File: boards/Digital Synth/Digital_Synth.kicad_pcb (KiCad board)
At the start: 2 copper layers, 109 parts, among them J1 AudioJack3, J2 AudioJack3, J3 DIN-5, J4 DIN-5, SW1 C3, SW10 A4, SW11 A#4, SW12 B4, SW13 C4, SW14 C#4, SW15 D4, SW16 D#4, SW17 E4, SW18 F4, SW19 F#4, SW2 C#3, SW20 G4, SW21 G#4, SW22 A5, SW23 A#4, SW24 B5, SW25 C5, SW3 D3, SW4 D#3, SW5 E3, SW6 F3, SW7 F#3, SW8 G3, SW9 G#3, U1 STM32F446RETx, U2 SN74LVC2G14, U3 PCM5101A, U4 6N138

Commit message: laid out keyboard
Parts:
- removed D31, D32, D33, D34, D35, D36, D37, D38, D39, D40, D41, D42, D43, D44, D45, D46, D47, D48, D49, D50, D51, D52, D53, D54, D55: D_Small, Diode_SMD:D_0805_2012Metric_Pad1.15x1.40mm_HandSolder
- removed R9: 220, Resistor_SMD:R_0805_2012Metric_Pad1.15x1.40mm_HandSolder
- removed SW1: C3, Keyswitches:Kailh_socket_MX
- removed SW10: A4, Keyswitches:Kailh_socket_MX
- removed SW11, SW23: A#4, Keyswitches:Kailh_socket_MX
- removed SW12: B4, Keyswitches:Kailh_socket_MX
- removed SW13: C4, Keyswitches:Kailh_socket_MX
- removed SW14: C#4, Keyswitches:Kailh_socket_MX
- removed SW15: D4, Keyswitches:Kailh_socket_MX
- removed SW16: D#4, Keyswitches:Kailh_socket_MX
- removed SW17: E4, Keyswitches:Kailh_socket_MX
- removed SW18: F4, Keyswitches:Kailh_socket_MX
- removed SW19: F#4, Keyswitches:Kailh_socket_MX
- removed SW2: C#3, Keyswitches:Kailh_socket_MX
- removed SW20: G4, Keyswitches:Kailh_socket_MX
- removed SW21: G#4, Keyswitches:Kailh_socket_MX
- removed SW22: A5, Keyswitches:Kailh_socket_MX
- removed SW24: B5, Keyswitches:Kailh_socket_MX
- removed SW25: C5, Keyswitches:Kailh_socket_MX
- removed SW3: D3, Keyswitches:Kailh_socket_MX
- removed SW4: D#3, Keyswitches:Kailh_socket_MX
- removed SW5: E3, Keyswitches:Kailh_socket_MX
- removed SW6: F3, Keyswitches:Kailh_socket_MX
- removed SW7: F#3, Keyswitches:Kailh_socket_MX
- removed SW8: G3, Keyswitches:Kailh_socket_MX
- removed SW9: G#3, Keyswitches:Kailh_socket_MX
- removed U1: STM32F446RETx, Package_QFP:LQFP-64_10x10mm_P0.5mm
- added C1: 0.1uF, Capacitor_SMD:C_0603_1608Metric_Pad1.05x0.95mm_HandSolder, F.Cu at (78.1, -9.42)
- added C15: 0.1uF, Capacitor_SMD:C_0603_1608Metric_Pad1.05x0.95mm_HandSolder, B.Cu at (157.6, -9.27)
- added C17: 0.1uF, Capacitor_SMD:C_0603_1608Metric_Pad1.05x0.95mm_HandSolder, B.Cu at (154.9, -13.1)
- added C21: 0.1uF, Capacitor_SMD:C_0603_1608Metric_Pad1.05x0.95mm_HandSolder, B.Cu at (154.9, -18.0)
- added C26: 0.1uF, Capacitor_SMD:C_0603_1608Metric_Pad1.05x0.95mm_HandSolder, B.Cu at (157.1, -20.8)
- added C27: 0.1uF, Capacitor_SMD:C_0603_1608Metric_Pad1.05x0.95mm_HandSolder, B.Cu at (166.4, -18.4)
- added C28: 0.1uF, Capacitor_SMD:C_0603_1608Metric_Pad1.05x0.95mm_HandSolder, F.Cu at (78.7, -4.45)
- added C29: 0.1uF, Capacitor_SMD:C_0603_1608Metric_Pad1.05x0.95mm_HandSolder, F.Cu at (138.4, 21.0)
- added C3: 0.1uF, Capacitor_SMD:C_0603_1608Metric_Pad1.05x0.95mm_HandSolder, F.Cu at (115.1, -29.0)
- added C30: 0.1uF, Capacitor_SMD:C_0603_1608Metric_Pad1.05x0.95mm_HandSolder, F.Cu at (128.5, 20.3)
- added C6: 0.1uF, Capacitor_SMD:C_0603_1608Metric_Pad1.05x0.95mm_HandSolder, B.Cu at (106.3, -3.81)
- added J8: ISP, Connector_PinSocket_2.54mm:PinSocket_2x03_P2.54mm_Horizontal, F.Cu at (136.9, 5.97)
- added MX1: C3, Keyswitches:Kailh_socket_MX, F.Cu at (9.61, 50.2)
- added MX10: A4, Keyswitches:Kailh_socket_MX, F.Cu at (104.9, 50.2)
- added MX11: A#4, Keyswitches:Kailh_socket_MX, F.Cu at (114.4, 26.4)
- added MX12: B4, Keyswitches:Kailh_socket_MX, F.Cu at (123.9, 50.2)
- added MX13: C4, Keyswitches:Kailh_socket_MX, F.Cu at (143.0, 50.2)
- added MX14: C#4, Keyswitches:Kailh_socket_MX, F.Cu at (152.5, 26.4)
- added MX15: D4, Keyswitches:Kailh_socket_MX, F.Cu at (162.0, 50.2)
- added MX16: D#4, Keyswitches:Kailh_socket_MX, F.Cu at (171.5, 26.4)
- added MX17: E4, Keyswitches:Kailh_socket_MX, F.Cu at (181.1, 50.2)
- added MX18: F4, Keyswitches:Kailh_socket_MX, F.Cu at (200.1, 50.2)
- added MX19: F#4, Keyswitches:Kailh_socket_MX, F.Cu at (209.6, 26.4)
- added MX2: C#3, Keyswitches:Kailh_socket_MX, F.Cu at (19.1, 26.4)
- added MX20: G4, Keyswitches:Kailh_socket_MX, F.Cu at (219.2, 50.2)
- added MX21: G#4, Keyswitches:Kailh_socket_MX, F.Cu at (228.7, 26.4)
- added MX22: A5, Keyswitches:Kailh_socket_MX, F.Cu at (238.2, 50.2)
- added MX23: A#4, Keyswitches:Kailh_socket_MX, F.Cu at (247.7, 26.4)
- added MX24: B5, Keyswitches:Kailh_socket_MX, F.Cu at (257.3, 50.2)
- added MX25: C5, Keyswitches:Kailh_socket_MX, F.Cu at (276.3, 50.2)
- added MX3: D3, Keyswitches:Kailh_socket_MX, F.Cu at (28.7, 50.2)
- added MX4: D#3, Keyswitches:Kailh_socket_MX, F.Cu at (38.2, 26.4)
- added MX5: E3, Keyswitches:Kailh_socket_MX, F.Cu at (47.7, 50.2)
- added MX6: F3, Keyswitches:Kailh_socket_MX, F.Cu at (66.8, 50.2)
- added MX7: F#3, Keyswitches:Kailh_socket_MX, F.Cu at (76.3, 26.4)
- added MX8: G3, Keyswitches:Kailh_socket_MX, F.Cu at (85.8, 50.2)
- added MX9: G#3, Keyswitches:Kailh_socket_MX, F.Cu at (95.3, 26.4)
- added R1: 220, Resistor_SMD:R_0805_2012Metric_Pad1.15x1.40mm_HandSolder, F.Cu at (73.6, -9.20)
- added R12: 100k, Resistor_SMD:R_0805_2012Metric_Pad1.15x1.40mm_HandSolder, F.Cu at (158.9, -26.5)
- added R2: 10k, Resistor_SMD:R_0805_2012Metric_Pad1.15x1.40mm_HandSolder, F.Cu at (67.7, -4.55)
- added U5: STM32F405RGTx, Package_QFP:LQFP-64_10x10mm_P0.5mm, F.Cu at (160.7, -15.0)
- added U6: ATtiny167-XU, Package_SO:TSSOP-20_4.4x6.5mm_P0.65mm, B.Cu at (133.1, 21.1)
- C25: moved to B.Cu
- R5: value 220 -> 1k
- R6: value 10k -> 220
- R7: value 1k -> 220
- R8: value 220 -> 4.7k
- U2: value SN74LVC2G14 -> 6N138; footprint Package_TO_SOT_SMD:SOT-23-6_Handsoldering -> Package_DIP:SMDIP-8_W7.62mm
- U4: value 6N138 -> SN74LVC2G14; footprint Package_DIP:SMDIP-8_W7.62mm -> Package_TO_SOT_SMD:SOT-23-6_Handsoldering
- moved U4 272.3 mm to (31.2, -19.8), turned to 0 degrees
- moved R6 271.5 mm to (26.2, -19.8)
- moved J4 247.6 mm to (31.3, -34.5)
- moved J3 246.7 mm to (57.7, -34.5)
- moved C19 236.4 mm to (236.0, -18.3)
- moved D1 236.4 mm to (223.9, -19.1)
- moved D3 236.4 mm to (226.4, -19.1)
- moved C14 236.4 mm to (241.0, -21.1)
- moved C16 236.4 mm to (271.4, -43.7)
- moved C18 236.4 mm to (269.2, -29.2)
- moved C20 236.4 mm to (261.9, -43.7)
- moved C22 236.4 mm to (269.2, -21.6)
- moved C23 236.4 mm to (232.3, -17.6)
- moved C24 236.4 mm to (232.3, -14.1)
- moved C4 236.4 mm to (261.6, -30.5)
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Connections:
- C25 pad 1: GND -> +3V3
- C25 pad 2: +5V -> GND
- D17 pad 1: row0 -> row2
- D18 pad 1: row1 -> row3
- D19 pad 1: row0 -> row2
- D20 pad 1: row1 -> row3
- D21 pad 1: row0 -> row2
- D22 pad 1: row0 -> row2
- D23 pad 1: row1 -> row3
- D24 pad 1: row0 -> row2
- D25 pad 1: row1 -> row3
- D26 pad 1: row0 -> row2
- D27 pad 1: row1 -> row3
- D28 pad 1: row0 -> row2
- D29 pad 1: row0 -> row3
- R5 pad 1: Net-(D30-Pad1) -> +3V3
- R5 pad 2: Net-(J3-Pad4) -> RXD
- R6 pad 1: Net-(R6-Pad1) -> Net-(J4-Pad4)
- R6 pad 2: GND -> Net-(R6-Pad2)
- R7 pad 1: +3V3 -> +5V
- R7 pad 2: RXD -> Net-(J4-Pad5)
- R8 pad 1: Net-(J4-Pad4) -> +3V3
- R8 pad 2: Net-(R8-Pad2) -> NRST
- U2 pad 1: TXD -> Net-(U2-Pad1)
- U2 pad 2: GND -> Net-(D30-Pad1)
- U2 pad 3: Net-(U2-Pad3) -> Net-(D30-Pad2)
- U2 pad 4: Net-(R8-Pad2) -> Net-(U2-Pad4)
- U2 pad 5: +5V -> GND
- U2 pad 6: Net-(U2-Pad3) -> RXD
- U4 pad 1: Net-(U4-Pad1) -> TXD
- U4 pad 2: Net-(D30-Pad1) -> GND
- U4 pad 3: Net-(D30-Pad2) -> Net-(U4-Pad3)
- U4 pad 4: Net-(U4-Pad4) -> Net-(R6-Pad2)
- U4 pad 5: GND -> +5V
- U4 pad 6: RXD -> Net-(U4-Pad3)
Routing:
- net col5: track 0.00 -> 313.1 mm, vias 0 -> 2
- net col3: track 0.00 -> 212.6 mm, vias 0 -> 6
- net col2: track 0.00 -> 210.7 mm, vias 0 -> 4
- net col4: track 0.00 -> 203.1 mm, vias 0 -> 6
- net col1: track 0.00 -> 196.6 mm, vias 0 -> 6
- net col0: track 0.00 -> 195.1 mm, vias 0 -> 3
- net row3: track 0.00 -> 162.6 mm, vias 0 -> 2
- net col6: track 0.00 -> 161.6 mm, vias 0 -> 2
- net row2: track 0.00 -> 160.1 mm, vias 0 -> 2
- net row0: track 0.00 -> 156.2 mm, vias 0 -> 2
- net row1: track 0.00 -> 119.4 mm, vias 0 -> 2
- net +5V: track 36.0 -> 0.00 mm
- net NRST: track 0.00 -> 33.8 mm, vias 0 -> 3
- net Net-(D30-Pad1): track 14.9 -> 0.00 mm
- net Net-(D30-Pad2): track 13.5 -> 0.00 mm
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- added copper zone on F.Cu, net +3V3

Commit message: finished routing to avr
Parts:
- removed REF**: Stabilizer_MX_2u, Keyswitches:Stabilizer_MX_2u
- added J6: JTAG, Connector_PinSocket_2.54mm:PinSocket_1x04_P2.54mm_Vertical, F.Cu at (167.1, 50.5)
- C1, C28: moved to B.Cu
- J8: footprint Connector_PinSocket_2.54mm:PinSocket_2x03_P2.54mm_Horizontal -> Connector_PinSocket_2.54mm:PinSocket_2x03_P2.54mm_Vertical
- moved R5 92.5 mm to (47.5, 59.4)
- moved C19 82.0 mm to (226.8, 63.2)
- moved D1 82.0 mm to (214.8, 62.5)
- moved D3 82.0 mm to (217.3, 62.5)
- moved U3 82.0 mm to (233.4, 65.0)
- moved C14 82.0 mm to (231.9, 60.5)
- moved C23 82.0 mm to (223.1, 63.9)
- moved C7 82.0 mm to (239.9, 63.8)
- moved C8 82.0 mm to (226.8, 60.5)
- moved D2 82.0 mm to (214.8, 58.7)
- moved D4 82.0 mm to (217.3, 58.7)
- moved R3 82.0 mm to (226.8, 64.9)
- moved R4 82.0 mm to (226.8, 66.4)
- moved C24 82.0 mm to (223.1, 67.4)
- moved D30 81.4 mm to (50.0, 45.2), turned to 180 degrees
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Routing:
- net Net-(D30-Pad1): track 0.00 -> 15.5 mm
- net Net-(D30-Pad2): track 0.00 -> 12.7 mm
- net GND: track 13.5 -> 25.1 mm, vias 9 -> 17
- net +5V: track 0.00 -> 11.4 mm, vias 0 -> 2
- net Net-(R6-Pad2): track 0.00 -> 8.38 mm
- net Net-(J4-Pad4): track 0.00 -> 8.27 mm
- net Net-(J4-Pad5): track 0.00 -> 7.96 mm
- net Net-(J3-Pad4): track 0.00 -> 7.05 mm
- net SPI_AVR_MISO: track 0.00 -> 4.35 mm
- net Net-(U4-Pad3): track 0.00 -> 4.16 mm
- net RXD: track 0.00 -> 3.40 mm
- net Net-(R2-Pad1): track 0.00 -> 3.31 mm
- net NRST: track 33.8 -> 35.8 mm
- net col5: track 313.1 -> 314.1 mm

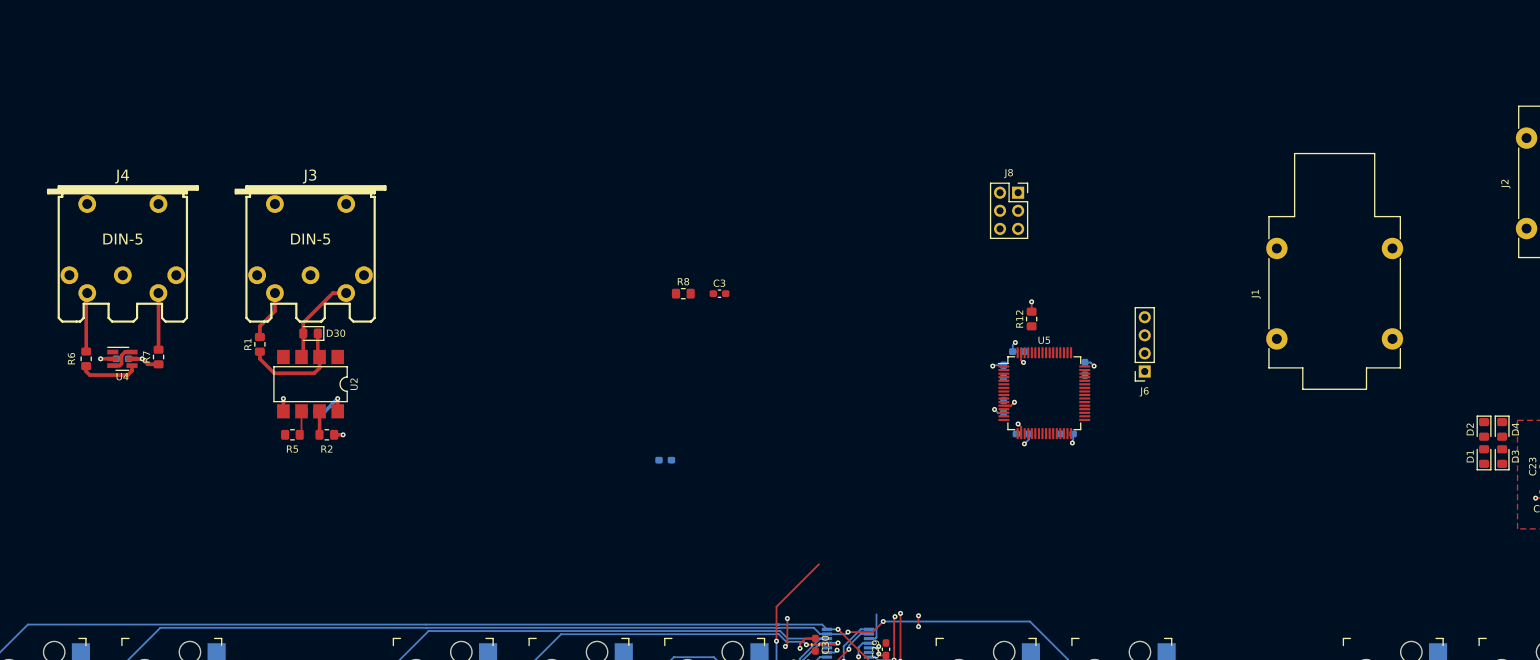
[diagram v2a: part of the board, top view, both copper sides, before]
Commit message: added display
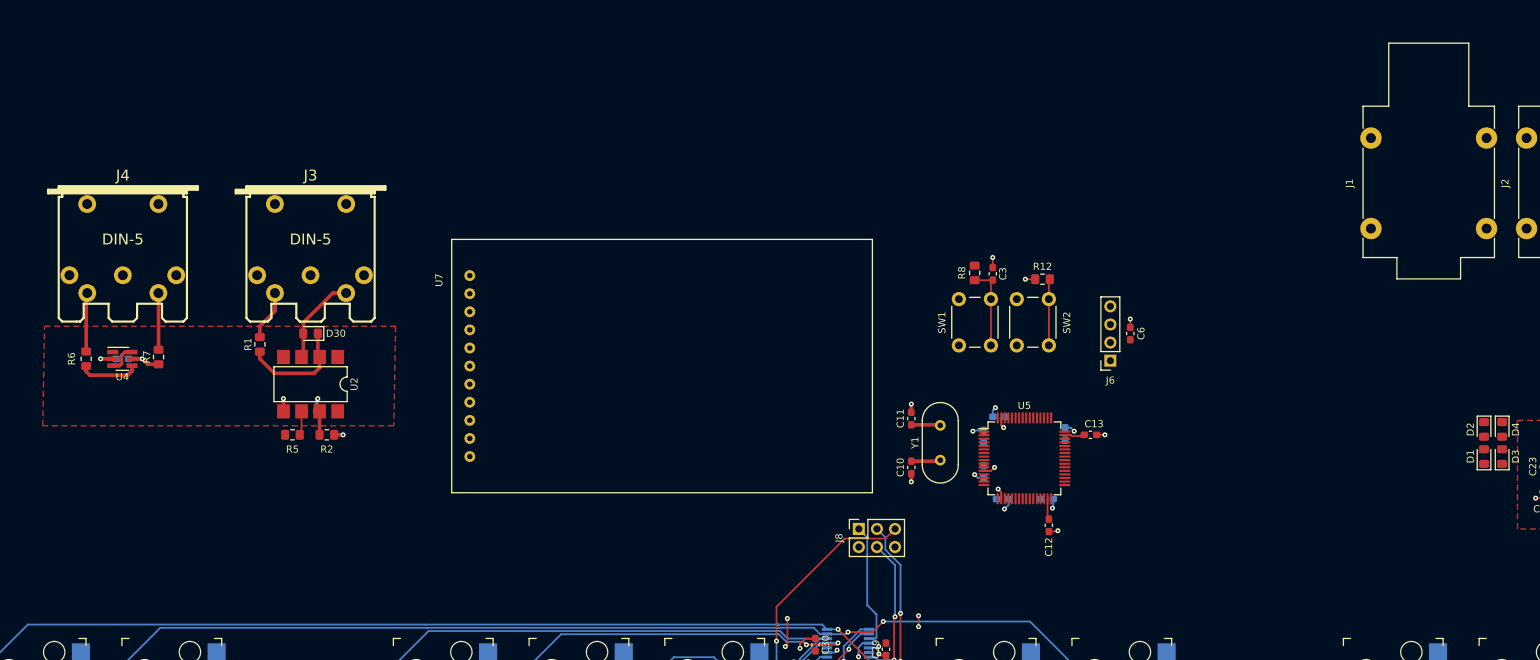
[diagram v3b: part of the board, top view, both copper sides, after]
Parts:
- added C10: 22pF, Capacitor_SMD:C_0603_1608Metric_Pad1.05x0.95mm_HandSolder, F.Cu at (134.4, 64.0)
- added C11: 22pF, Capacitor_SMD:C_0603_1608Metric_Pad1.05x0.95mm_HandSolder, F.Cu at (134.4, 57.1)
- added C12: 2.2uF, Capacitor_SMD:C_0603_1608Metric_Pad1.05x0.95mm_HandSolder, F.Cu at (153.7, 72.1)
- added C13: 2.2uF, Capacitor_SMD:C_0603_1608Metric_Pad1.05x0.95mm_HandSolder, F.Cu at (159.5, 59.4)
- added SW1: SW_Push, Button_Switch_THT:SW_PUSH_6mm, F.Cu at (145.5, 40.4)
- added SW2: SW_Push, Button_Switch_THT:SW_PUSH_6mm, F.Cu at (153.7, 40.4)
- added U7: Adafruit_2in, Display:Adafruit_2in, F.Cu at (72.4, 37.1)
- added Y1: 8MHz, Crystal:Crystal_HC49-U_Vertical, F.Cu at (138.4, 63.0)
- C6: moved to F.Cu
- moved C6 67.7 mm to (165.1, 45.2), turned to 270 degrees
- moved J8 52.2 mm to (127.0, 72.6), turned to 90 degrees
- moved R8 41.0 mm to (143.3, 36.7), turned to 270 degrees
- moved C3 38.5 mm to (145.8, 36.8), turned to 270 degrees
- moved J1 20.4 mm to (198.9, 30.5)
- moved C25 9.56 mm to (153.4, 68.5)
- moved C15 9.56 mm to (147.2, 68.5)
- moved C26 9.56 mm to (146.7, 56.9)
- moved C27 9.56 mm to (156.0, 59.3)
- moved C17 9.56 mm to (144.5, 64.6)
- moved C21 9.56 mm to (144.5, 59.7)
- moved U5 9.56 mm to (150.2, 62.7)
- moved R12 5.79 mm to (152.8, 37.6), turned to 180 degrees
- moved J6 5.06 mm to (162.3, 49.0)
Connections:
- net SDIO_CLK renamed Net-(U5-Pad53)
- net SDIO_D0 renamed Net-(U5-Pad39)
- net SDIO_D1 renamed Net-(U5-Pad40)
- net SDIO_D2 renamed Net-(U5-Pad51)
- net SDIO_D3 renamed Net-(U5-Pad52)
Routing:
- net NRST: track 35.8 -> 60.4 mm
- net SPI_AVR_SCK: track 11.5 -> 24.8 mm
- net SPI_AVR_MISO: track 4.35 -> 17.4 mm
- net SPI_AVR_MOSI: track 9.85 -> 20.7 mm
- net Net-(R12-Pad1): track 0.00 -> 9.35 mm
- net GND: track 25.1 -> 32.5 mm, vias 17 -> 23
- net Net-(C10-Pad1): track 0.00 -> 4.12 mm
- net Net-(C11-Pad1): track 0.00 -> 4.10 mm
- net +5V: track 11.4 -> 7.80 mm
- net Net-(C12-Pad1): track 0.00 -> 2.92 mm
- net Net-(C13-Pad1): track 0.00 -> 2.84 mm
- added copper zone on F.Cu, net +5V

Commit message: almost done with layout
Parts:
- removed D1, D2, D3, D4: D_Zener_Small_ALT, Diode_SMD:D_0805_2012Metric_Pad1.15x1.40mm_HandSolder
- removed SW2: SW_Push, Button_Switch_THT:SW_PUSH_6mm
- removed U7: Adafruit_2in, Display:Adafruit_2in
- added C2: 10uF, Capacitor_THT:CP_Radial_D5.0mm_P2.00mm, F.Cu at (198.6, 39.9)
- added C9: 10uF, Capacitor_THT:CP_Radial_D5.0mm_P2.00mm, F.Cu at (212.5, 42.0)
- added D31: Green, Diode_SMD:D_0805_2012Metric_Pad1.15x1.40mm_HandSolder, F.Cu at (251.5, 60.8)
- added D32: Green, Diode_SMD:D_0805_2012Metric_Pad1.15x1.40mm_HandSolder, F.Cu at (250.1, 59.4)
- added D33: Green, Diode_SMD:D_0805_2012Metric_Pad1.15x1.40mm_HandSolder, F.Cu at (205.0, 50.7)
- added J5: 5V IN, Connector_BarrelJack:BarrelJack_CUI_PJ-102AH_Horizontal, F.Cu at (205.6, 34.7)
- added J7: UART_Debug, Connector_PinHeader_2.54mm:PinHeader_1x02_P2.54mm_Vertical, F.Cu at (255.8, 81.8)
- added J9: UART_MIDI, Connector_PinHeader_2.54mm:PinHeader_1x02_P2.54mm_Vertical, F.Cu at (254.0, 67.1)
- added MXB1: SW_Push, Keyswitches:Kailh_socket_MX, F.Cu at (1.99, 37.9)
- added MXB2: SW_Push, Keyswitches:Kailh_socket_MX, F.Cu at (21.0, 37.9)
- added MXB3: SW_Push, Keyswitches:Kailh_socket_MX, F.Cu at (40.1, 37.9)
- added MXB4: SW_Push, Keyswitches:Kailh_socket_MX, F.Cu at (1.99, 56.9)
- added MXB5: SW_Push, Keyswitches:Kailh_socket_MX, F.Cu at (21.0, 56.9)
- added MXB6: SW_Push, Keyswitches:Kailh_socket_MX, F.Cu at (40.1, 56.9)
- added MXB7: SW_Push, Keyswitches:Kailh_socket_MX, F.Cu at (1.99, 76.0)
- added MXB8: SW_Push, Keyswitches:Kailh_socket_MX, F.Cu at (21.0, 76.0)
- added MXB9: SW_Push, Keyswitches:Kailh_socket_MX, F.Cu at (40.1, 76.0)
- added R10: 470, Resistor_SMD:R_0603_1608Metric_Pad1.05x0.95mm_HandSolder, F.Cu at (247.7, 62.2)
- added R11: 470, Resistor_SMD:R_0603_1608Metric_Pad1.05x0.95mm_HandSolder, F.Cu at (204.9, 48.8)
- added R13: R_Small, Resistor_SMD:R_0603_1608Metric_Pad1.05x0.95mm_HandSolder, F.Cu at (311.9, 46.7)
- added R9: 470, Resistor_SMD:R_0603_1608Metric_Pad1.05x0.95mm_HandSolder, F.Cu at (248.8, 63.4)
- added RV1: 10k, Potentiometer_THT:Hiletgo, F.Cu at (129.0, 39.6)
- added RV2: 10k, Potentiometer_THT:Hiletgo, F.Cu at (146.8, 39.6)
- added RV3: 10k, Potentiometer_THT:Hiletgo, F.Cu at (164.6, 39.6)
- added RV4: 10k, Potentiometer_THT:Hiletgo, F.Cu at (182.4, 39.6)
- added RV5: 10k, Potentiometer_THT:Hiletgo, F.Cu at (129.0, 62.5)
- added RV6: 10k, Potentiometer_THT:Hiletgo, F.Cu at (146.8, 62.5)
- added RV7: 10k, Potentiometer_THT:Hiletgo, F.Cu at (164.6, 62.5)
- added RV8: 10k, Potentiometer_THT:Hiletgo, F.Cu at (182.4, 62.5)
- added TP1: TestPoint, TestPoint:TestPoint_Pad_1.0x1.0mm, F.Cu at (231.1, 63.2)
- added U1: LM1117-3.3, Package_TO_SOT_SMD:SOT-223, F.Cu at (205.5, 42.8)
- added U8: Adafruit_2.4in, Display:Adafruit_2.4in, F.Cu at (60.8, 79.8)
- C23, C24: value 4.7nF -> 2.2nF; footprint Capacitor_SMD:C_0603_1608Metric_Pad1.05x0.95mm_HandSolder -> Capacitor_SMD:C_1206_3216Metric
- D10, D11, D12, D13, D14, D15, D16, D17, D18, D19, D20, D21, D22, D23, D24, D25, D26, D27, D28, D29, D30, D5, D6, D7, D8, D9: footprint Diode_SMD:D_0805_2012Metric_Pad1.15x1.40mm_HandSolder -> Diode_SMD:D_SOD-323
- J1: value AudioJack3 -> LOUT; footprint Connector_Audio_Ext:Jack_6.35mm_Neutrik_NMJ4HFD2_Horizontal -> Connector_Audio:Jack_3.5mm_CUI_SJ1-3533NG_Horizontal
- J2: value AudioJack3 -> ROUT; footprint Connector_Audio_Ext:Jack_6.35mm_Neutrik_NMJ4HFD2_Horizontal -> Connector_Audio:Jack_3.5mm_CUI_SJ1-3533NG_Horizontal
- J3: value DIN-5 -> MIDI IN; footprint Connector_Audio_Ext:MIDI_DIN5 -> Connector_Audio:Jack_3.5mm_CUI_SJ1-3533NG_Horizontal
- J4: value DIN-5 -> MIDI OUT; footprint Connector_Audio_Ext:MIDI_DIN5 -> Connector_Audio:Jack_3.5mm_CUI_SJ1-3533NG_Horizontal
- R1, R12, R2, R5, R6, R7, R8: footprint Resistor_SMD:R_0805_2012Metric_Pad1.15x1.40mm_HandSolder -> Resistor_SMD:R_0603_1608Metric_Pad1.05x0.95mm_HandSolder
- moved C3 234.4 mm to (378.1, 68.6)
- moved R8 234.4 mm to (375.5, 68.5)
- moved SW1 234.4 mm to (377.8, 72.1)
- moved R6 200.8 mm to (219.3, 44.8)
- moved J4 200.5 mm to (224.0, 26.2), turned to 0 degrees
- moved C28 200.2 mm to (223.8, 44.8)
- moved U4 200.2 mm to (223.8, 44.8)
- moved R7 199.0 mm to (227.7, 44.6)
- moved R1 187.9 mm to (230.8, 41.4), turned to 180 degrees
- moved R5 185.1 mm to (232.5, 54.9)
- moved R2 185.0 mm to (237.2, 54.9)
- moved C1 184.9 mm to (234.9, 52.5)
- moved D30 184.9 mm to (234.9, 41.5)
- moved U2 184.9 mm to (234.9, 48.6)
- moved J3 184.4 mm to (234.3, 26.2), turned to 0 degrees
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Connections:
- J8 pad 1: SPI_AVR_MISO -> SPI2_MISO
- J8 pad 2: Net-(D34-Pad2) -> +3V3
- J8 pad 3: SPI_AVR_SCK -> SPI2_SCK
- J8 pad 4: SPI_AVR_MOSI -> SPI2_MOSI
- R1 pad 2: Net-(J3-Pad4) -> Net-(J3-PadR)
- R5 pad 2: RXD -> RX_MIDI
- R6 pad 1: Net-(J4-Pad4) -> Net-(J4-PadR)
- R7 pad 2: Net-(J4-Pad5) -> Net-(J4-PadT)
- U2 pad 6: RXD -> RX_MIDI
- U3 pad 11: Net-(U3-Pad11) -> GND
- U3 pad 17: MUTE -> +3V3
- U4 pad 1: TXD -> TX_MIDI
- U5 pad 10: Net-(U5-Pad10) -> B8
- U5 pad 11: Net-(U5-Pad11) -> B9
- U5 pad 14: Net-(U5-Pad14) -> RV1
- U5 pad 15: Net-(U5-Pad15) -> RV2
- U5 pad 16: Net-(U5-Pad16) -> RV3
- U5 pad 17: Net-(U5-Pad17) -> RV4
- U5 pad 2: Net-(U5-Pad2) -> B3
- U5 pad 20: Net-(U5-Pad20) -> RV5
- U5 pad 21: Net-(U5-Pad21) -> RV6
- U5 pad 22: Net-(U5-Pad22) -> RV7
- U5 pad 23: Net-(U5-Pad23) -> RV8
- U5 pad 24: Net-(U5-Pad24) -> Y+
- U5 pad 25: Net-(U5-Pad25) -> X+
- U5 pad 26: Net-(U5-Pad26) -> Y-
- U5 pad 27: Net-(U5-Pad27) -> X-
- U5 pad 29: Net-(U5-Pad29) -> TX_Debug
- U5 pad 3: Net-(U5-Pad3) -> B4
- U5 pad 30: Net-(U5-Pad30) -> RX_Debug
- U5 pad 33: WS -> SPI2_CS
- U5 pad 34: BCK -> SPI2_SCK
- U5 pad 35: Net-(U5-Pad35) -> SPI2_MISO
- U5 pad 36: SD -> SPI2_MOSI
- U5 pad 37: MCK -> Net-(U5-Pad37)
- U5 pad 38: Net-(U5-Pad38) -> MCK
- U5 pad 4: Net-(U5-Pad4) -> B5
- U5 pad 42: Net-(U5-Pad42) -> TX_MIDI
- U5 pad 43: Net-(U5-Pad43) -> RX_MIDI
- U5 pad 50: Net-(U5-Pad50) -> WS
- U5 pad 51: Net-(U5-Pad51) -> BCK
- U5 pad 53: Net-(U5-Pad53) -> SD
- U5 pad 54: SDIO_CMD -> DC
- U5 pad 55: Net-(U5-Pad55) -> SPI1_SCK
- U5 pad 56: Net-(U5-Pad56) -> SPI1_MISO
- U5 pad 57: Net-(U5-Pad57) -> SPI1_MOSI
- U5 pad 58: Net-(U5-Pad58) -> SPI1_CS2
- U5 pad 59: Net-(U5-Pad59) -> SPI1_CS1
- U5 pad 61: Net-(U5-Pad61) -> B1
- U5 pad 62: Net-(U5-Pad62) -> B2
- U5 pad 8: Net-(U5-Pad8) -> B6
- U5 pad 9: Net-(U5-Pad9) -> B7
- U6 pad 3: SPI_AVR_MISO -> SPI2_MISO
- U6 pad 7: SPI_AVR_MOSI -> SPI2_MOSI
- U6 pad 8: SPI_AVR_SCK -> SPI2_SCK
- U6 pad 9: SPI_AVR_CS -> SPI2_CS
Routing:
- net +3V3: track 11.9 -> 46.8 mm, vias 8 -> 7
- net NRST: track 60.4 -> 34.4 mm
- net SPI_AVR_SCK: track 24.8 -> 0.00 mm, vias 2 -> 0
- net SPI_AVR_MOSI: track 20.7 -> 0.00 mm, vias 2 -> 0
- net SPI_AVR_MISO: track 17.4 -> 0.00 mm
- net Net-(C23-Pad2): track 0.00 -> 16.6 mm
- net Net-(C24-Pad2): track 0.00 -> 16.3 mm
- net Net-(J4-PadT): track 0.00 -> 16.0 mm
- net Net-(J4-PadR): track 0.00 -> 12.7 mm
- net SPI2_SCK: track 0.00 -> 11.5 mm, vias 0 -> 2
- net Net-(J3-PadR): track 0.00 -> 10.0 mm
- net SPI2_MOSI: track 0.00 -> 9.85 mm, vias 0 -> 2
- net GND: track 32.5 -> 42.3 mm, vias 23 -> 40
- net +5V: track 7.80 -> 17.2 mm
- net Net-(J4-Pad4): track 8.27 -> 0.00 mm
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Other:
- board outline added: 290.8 x 106.7 mm
- net class Default: clearance 0.2 -> 0.199898
- rule trace_clearance: 0.2 -> 0.199898

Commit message: finished layout
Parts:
- added REF**: MountingHole_3.2mm_M3, MountingHole:MountingHole_3.2mm_M3, F.Cu at (50.0, 27.4)
- added REF**: MountingHole_3.2mm_M3, MountingHole:MountingHole_3.2mm_M3, F.Cu at (-6.35, 128.0)
- added REF**: MountingHole_3.2mm_M3, MountingHole:MountingHole_3.2mm_M3, F.Cu at (278.4, 128.0)
- added REF**: MountingHole_3.2mm_M3, MountingHole:MountingHole_3.2mm_M3, F.Cu at (278.4, 27.4)
- added REF**: MountingHole_3.2mm_M3, MountingHole:MountingHole_3.2mm_M3, F.Cu at (-6.35, 27.4)
- moved SW1 164.0 mm to (213.8, 70.4), turned to 225 degrees
- moved C3 161.6 mm to (216.5, 68.1), turned to 225 degrees
- moved R8 160.8 mm to (214.8, 66.2), turned to 225 degrees
- moved C11 100.1 mm to (221.4, 73.5), turned to 270 degrees
- moved Y1 97.6 mm to (225.0, 67.6), turned to 270 degrees
- moved C10 96.9 mm to (221.4, 66.8), turned to 90 degrees
- moved R13 86.8 mm to (228.7, 71.6), turned to 270 degrees
- moved TP1 14.2 mm to (243.7, 56.7), turned to 0 degrees
- moved R12 12.7 mm to (241.0, 56.7), turned to 180 degrees
- moved D32 9.62 mm to (256.6, 66.5), turned to 180 degrees
- moved D31 9.21 mm to (256.6, 68.5), turned to 180 degrees
- moved C13 7.79 mm to (252.8, 64.6), turned to 0 degrees
- moved R10 6.94 mm to (252.9, 66.8), turned to 0 degrees
- moved R9 6.49 mm to (252.9, 68.4), turned to 0 degrees
- moved C12 6.02 mm to (246.5, 80.0), turned to 0 degrees
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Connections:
- U3 pad 12: MCLK -> MCK
- U5 pad 14: RV1 -> RV4
- U5 pad 15: RV2 -> RV3
- U5 pad 16: RV3 -> RV2
- U5 pad 17: RV4 -> RV1
- U5 pad 50: WS -> LRCLK
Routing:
- net B7: track 0.00 -> 250.9 mm, vias 0 -> 1
- net B1: track 0.00 -> 248.4 mm, vias 0 -> 1
- net B4: track 0.00 -> 238.9 mm, vias 0 -> 1
- net B8: track 0.00 -> 231.7 mm, vias 0 -> 1
- net B2: track 0.00 -> 228.4 mm, vias 0 -> 1
- net B5: track 0.00 -> 219.6 mm, vias 0 -> 1
- net B9: track 0.00 -> 212.5 mm, vias 0 -> 1
- net B6: track 0.00 -> 205.1 mm, vias 0 -> 1
- net B3: track 0.00 -> 205.0 mm, vias 0 -> 1
- net SPI1_SCK: track 0.00 -> 188.5 mm, vias 0 -> 1
- net DC: track 0.00 -> 186.6 mm, vias 0 -> 2
- net SPI1_MISO: track 0.00 -> 184.8 mm, vias 0 -> 1
- net SPI1_MOSI: track 0.00 -> 181.1 mm, vias 0 -> 1
- net SPI1_CS2: track 0.00 -> 177.3 mm, vias 0 -> 1
- net +5V: track 17.2 -> 192.9 mm, vias 2 -> 4
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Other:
- outline, holes or cut-outs redrawn
